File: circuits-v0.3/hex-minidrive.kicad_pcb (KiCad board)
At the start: 4 copper layers, 18 x 48 mm, 81 parts, among them X1 16MHz

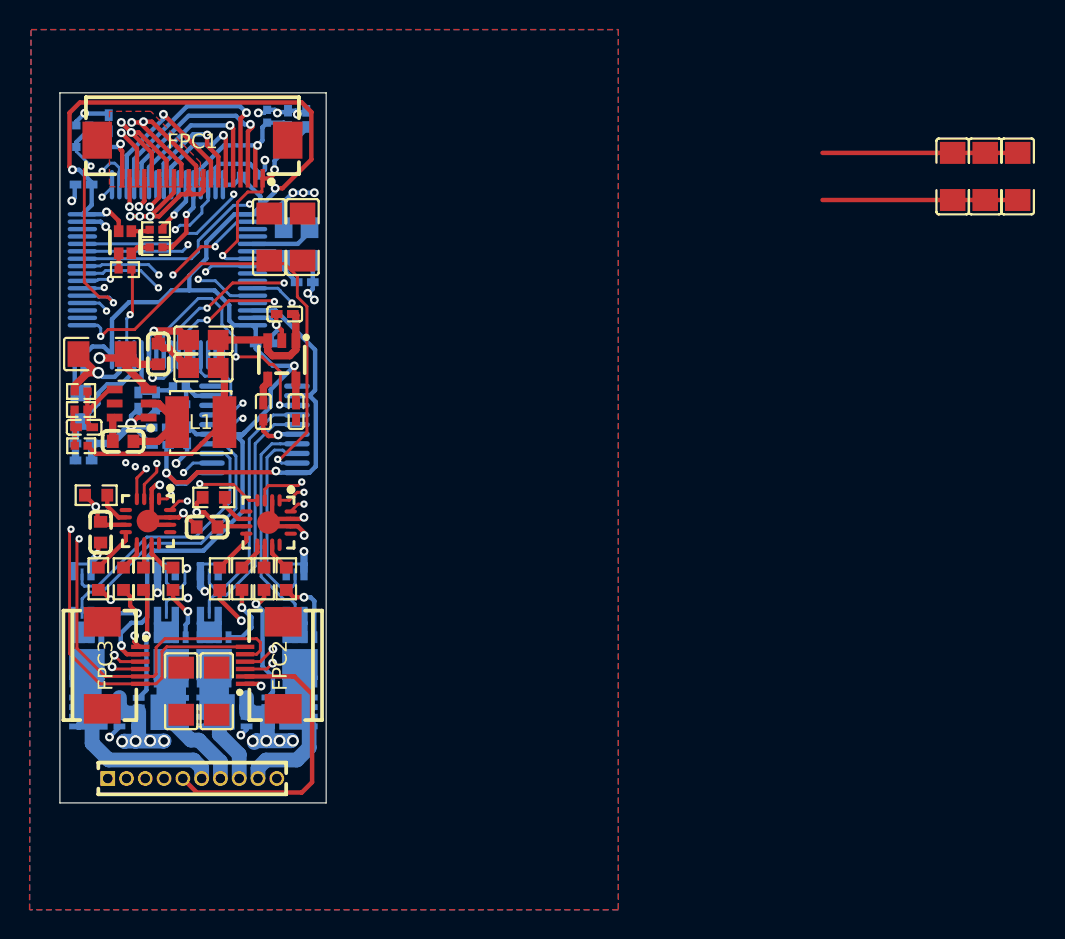
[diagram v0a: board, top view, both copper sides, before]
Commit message: Finished v0.3 circuit layout.
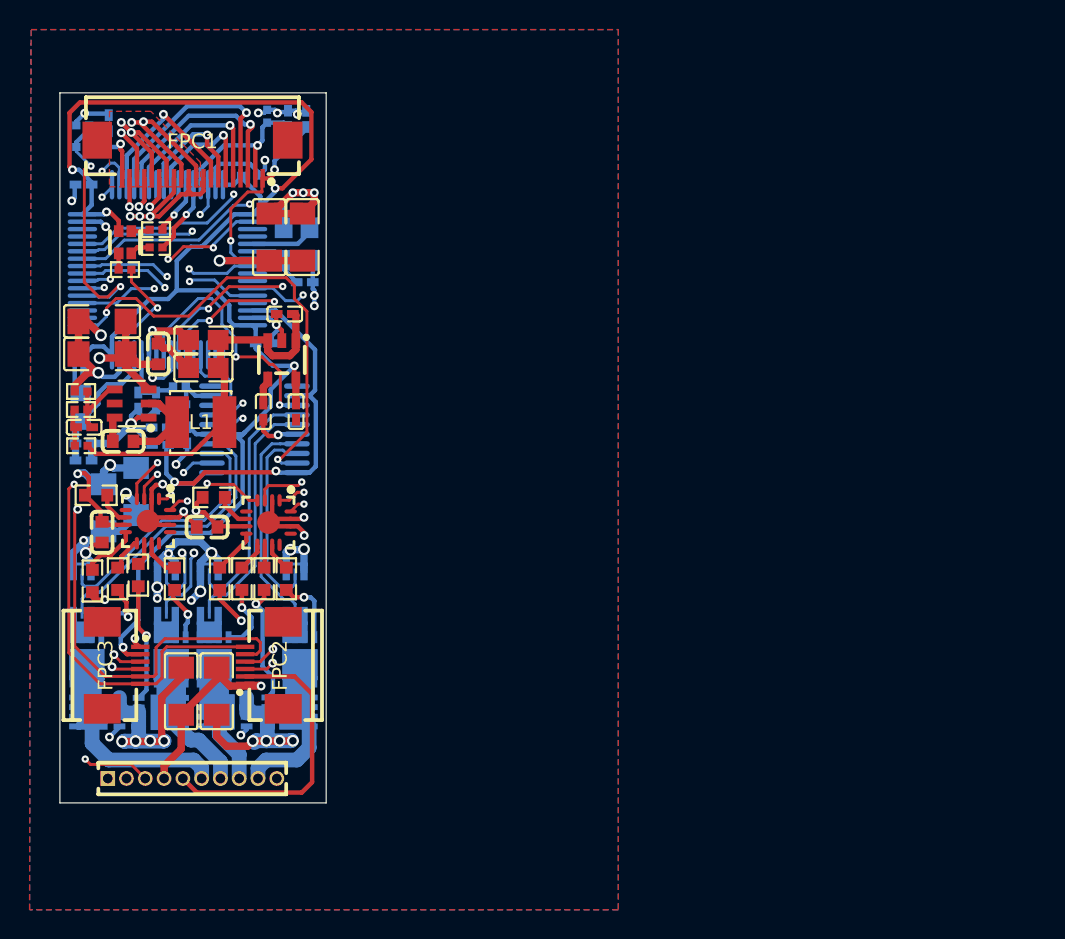
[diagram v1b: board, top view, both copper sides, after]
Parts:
- C4, C6: moved to B.Cu
- moved C6 63.3 mm to (24.1, 47.0), turned to 90 degrees
- moved C4 61.6 mm to (21.9, 48.0), turned to 90 degrees
- moved C5 60.5 mm to (21.9, 35.5), turned to 0 degrees
- moved R202 0.43 mm to (24.3, 52.6)
- moved R102 0.43 mm to (21.2, 53.0)
- moved R101 0.40 mm to (22.9, 52.9)
- moved C501 0.10 mm to (21.9, 49.7)
- moved R201 0.10 mm to (26.8, 52.9)
- turned C1 to 90 degrees
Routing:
- net GND: track 118.9 -> 154.2 mm, vias 34 -> 42
- net VCC: track 72.8 -> 90.5 mm, vias 17 -> 19
- net TIM1_CH2N: track 16.8 -> 24.9 mm
- net TIM1_CH3N: track 28.1 -> 25.0 mm
- net 3V3: track 148.1 -> 145.2 mm
- net /Gate-1-Positive: track 14.4 -> 12.1 mm
- net TIM1_CH1: track 20.5 -> 22.3 mm
- net TIM2_CH3/BLUE_LED: track 5.95 -> 7.47 mm
- net ADC2_IN15/VOLTAGE: track 18.1 -> 19.2 mm
- net TIM1_CH4: track 18.9 -> 20.0 mm
- net I2C3_SCL: track 35.3 -> 36.3 mm, vias 3 -> 2
- net TIM1_CH1N: track 23.5 -> 24.4 mm
- net ADC2_IN14/M4_CURRENT: track 32.5 -> 31.6 mm
- net NRST: track 14.0 -> 13.1 mm
- net I2C3_SDA: track 35.4 -> 36.2 mm, vias 3 -> 2
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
